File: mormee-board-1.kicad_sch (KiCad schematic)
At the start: 0 parts

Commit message: All key features are in the schematic.
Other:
- added sheet Battery (battery.kicad_sch)
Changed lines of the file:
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@@
+	)
+	(sheet
+		(at 191.77 45.72)
+		(size 26.67 24.13)
+		(exclude_from_sim no)
+		(in_bom yes)
+		(on_board yes)
+		(dnp no)
+		(fields_autoplaced yes)
+		(stroke
+			(width 0.1524)
+			(type solid)
+		)
+		(fill
+			(color 0 0 0 0.0000)
+		)
+		(property "Sheetname" "Battery"
+			(at 191.77 45.0084 0)
+			(effects
+				(font
+					(size 1.27 1.27)
+				)
+				(justify left bottom)
+			)
+		)
+		(property "Sheetfile" "battery.kicad_sch"
+			(at 191.77 70.4346 0)
+			(effects
+				(font
+					(size 1.27 1.27)
+				)
+				(justify left top)
+			)
+		)
+		(instances
+			(project "mormee-board-1"
+				(path "/d2af8ba6-fbfa-439f-91d9-67827f3f2396"
+					(page "6")
+				)
+			)
+		)
 	)
 	(sheet

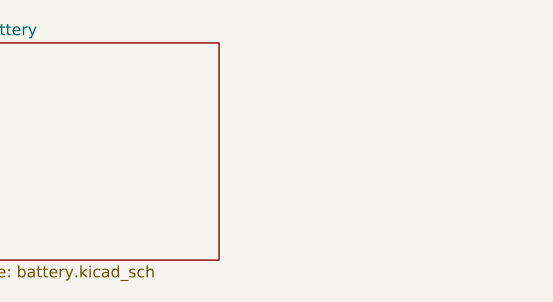
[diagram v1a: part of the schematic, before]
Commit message: All fiducials and mounting holes placed. Except one hole, which I'll try to place. WIP
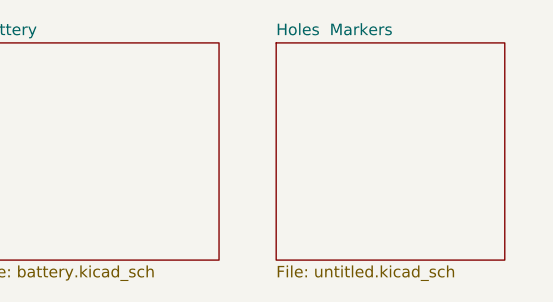
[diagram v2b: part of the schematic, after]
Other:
- added sheet Holes  Markers (untitled.kicad_sch)
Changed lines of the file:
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@@
+	)
+	(sheet
+		(at 224.79 45.72)
+		(size 25.4 24.13)
+		(exclude_from_sim no)
+		(in_bom yes)
+		(on_board yes)
+		(dnp no)
+		(fields_autoplaced yes)
+		(stroke
+			(width 0.1524)
+			(type solid)
+		)
+		(fill
+			(color 0 0 0 0.0000)
+		)
+		(property "Sheetname" "Holes  Markers"
+			(at 224.79 45.0084 0)
+			(effects
+				(font
+					(size 1.27 1.27)
+				)
+				(justify left bottom)
+			)
+		)
+		(property "Sheetfile" "untitled.kicad_sch"
+			(at 224.79 70.4346 0)
+			(effects
+				(font
+					(size 1.27 1.27)
+				)
+				(justify left top)
+			)
+		)
+		(instances
+			(project "mormee-board-1"
+				(path "/d2af8ba6-fbfa-439f-91d9-67827f3f2396"
+					(page "7")
+				)
+			)
+		)
 	)
 	(sheet
